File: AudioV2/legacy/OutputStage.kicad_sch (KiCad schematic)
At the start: 7 parts, among them SW501 DEST L (PHONE/MUTE/LINE), SW502 DEST R (PHONE/MUTE/LINE)

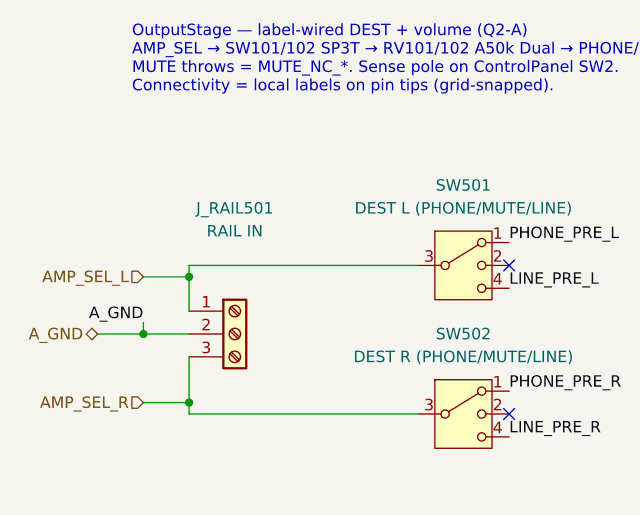
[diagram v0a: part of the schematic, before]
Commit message: AudioV2: レビュー指摘 3・4 を反映（OCP/容量の訂正、旧注釈10個の掃除、J_RAIL501 の Value）
レビューコメント（電源差し替えと U1604 削除の主経路は成立、残る4点は方針/文書/配線手順）
のうち、判断を要しない 3 と 4 を直した。1 と 2 は NOW.md に未判断として置いた。

## 3. DECISIONS の記述訂正（自分の誤り2件）

- U201 の OCP を「150% Io」と書いていたが、それは REC10K の値。
  REC20K-2415DZ は **225% of rated IOUT**（nom. VIN=48VDC、Recom_REC20K-Z_Rev3-2025.pdf）
- 「+15V/-15V とも 259.8µF」は差し替え時点の値。同日の U1604 削除で C1606/C1619
  （計 20.2µF）が中間レールから +15V に載り、いまは **+15V 280.0µF / -15V 259.8µF**。
  REC10K の Cout ±270µF に対して 96% → **103.7% で上限超え**。REC20K の理由②は
  差し替え後にさらに強まった

## 4. MeasureControl の旧注釈を掃除

26 個の text のうち 10 個が 2026-09-01 の再アノテーション前の designator のままだった。
うち3つは内容が現物と食い違っていた:

- [3][4] 電源系の注釈が **削除済みの U1604(MBC2596) の構成を今も説明**していた
  → ⑥-A 後の実配線（ADC の LDO は +15V 直結）に書き直し
- [11] GND の注釈が **NetTie の対応を現物と逆に**書いていた
  （旧「NT702=A_GND─ADC_GND / NT701=ADC_GND_IN─D_GND」→ 現物は NT1601 / NT1602）
  → NT1603 の新設と「3つを近接させる」も足した

残り7個は designator の置換のみ（回路図で1個ずつ対応を確定してから）:
  U704→U1607 U706→U1603 U707→U1606 U708→U1609 U709→U1605
  Y701→Y1601 D701→D1601 A701→A1601
  R717→R1620 R718→R1604 R719→R1611 R720→R1605
  C745→C1614（TPS3307 VDD） C740→C1633（XC8107 CIN） C739→C1631（XC8107 CL）
  NT701→NT1602 NT702→NT1601

同座標・同文の重複 2 組（[13][14] / [15][16]）を1つずつに。残る旧 designator は 0。

## J_RAIL501 の Value

「RAIL IN」→「AMP_SEL OUT」。実ネットは AMP_SEL_L / A_GND / AMP_SEL_R で、
娘基板がスロット直結になる前の名残だった。Description は前回直してある。
Value 変更なので PARTS.md を再生成した（BOM の行が変わる。netlist は変わらない）。

## 1・2 は NOW.md に未判断として置いた

1. ADC 枝の PPTC（旧 F1603）を戻すか — 既に記載あり
2. 計測側の電源端子 J1602/J1603 を残すか — **基板を分けるかの判断の下流**。
   分けないなら J1601 も含めて3個とも不要。分けるなら **J1603 のピン並びが J201 と逆**
   （J201=+15/GND/−15、J1603=−15/GND/+15。ピン番号どおりに繋ぐとレールが入れ替わる）。
   J1602 は F1601 が端子の外側に付いた行き止まりで、⑥-A 後は U1607 1個の 12V 入口

## 検証

  check_sexpr.py -q AudioV2   13 ファイル / 問題 0
  kicad-run.sh erc            11 件（変化なし）
  kicad-run.sh netlist        部品 370 個・重複 0・footprint 未設定 0（変化なし）
  sch_import --roundtrip      6/6 OK
  再生成の冪等性               バイト一致
  gen_parts_bom.py --check    OK

Co-Authored-By: Claude Fabl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
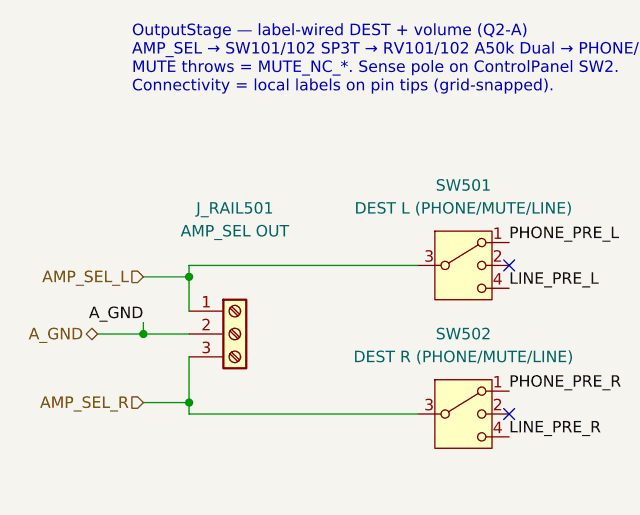
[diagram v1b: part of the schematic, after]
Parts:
- J_RAIL501: value RAIL IN -> AMP_SEL OUT
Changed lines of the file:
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@@
 			)
 		)
-		(property "Value" "RAIL IN"
+		(property "Value" "AMP_SEL OUT"
 			(at 36.83 48.26 0)
 			(show_name no)
@@
 			)
 		)
-		(property "Description" "選択された Amp 出力の取り出し端子。1=AMP_SEL_L / 2=A_GND / 3=AMP_SEL_R で、DEST スイッチ(SW501/SW502)の手前。Value の RAIL IN と旧記述の +12V/A_GND/-12V は、娘基板がスロット直結(J_PWR/J_ANA)になる前の名残で電源ではない。A_GND 極を持つ唯一の音声取り出し口。"
+		(property "Description" "選択された Amp 出力の取り出し端子。1=AMP_SEL_L / 2=A_GND / 3=AMP_SEL_R で、DEST スイッチ(SW501/SW502)の手前。旧 Value の RAIL IN と旧記述の +12V/A_GND/-12V は、娘基板がスロット直結(J_PWR/J_ANA)になる前の名残で電源ではない。A_GND 極を持つ唯一の音声取り出し口。"
 			(at -13.97 -62.23 0)
 			(hide yes)

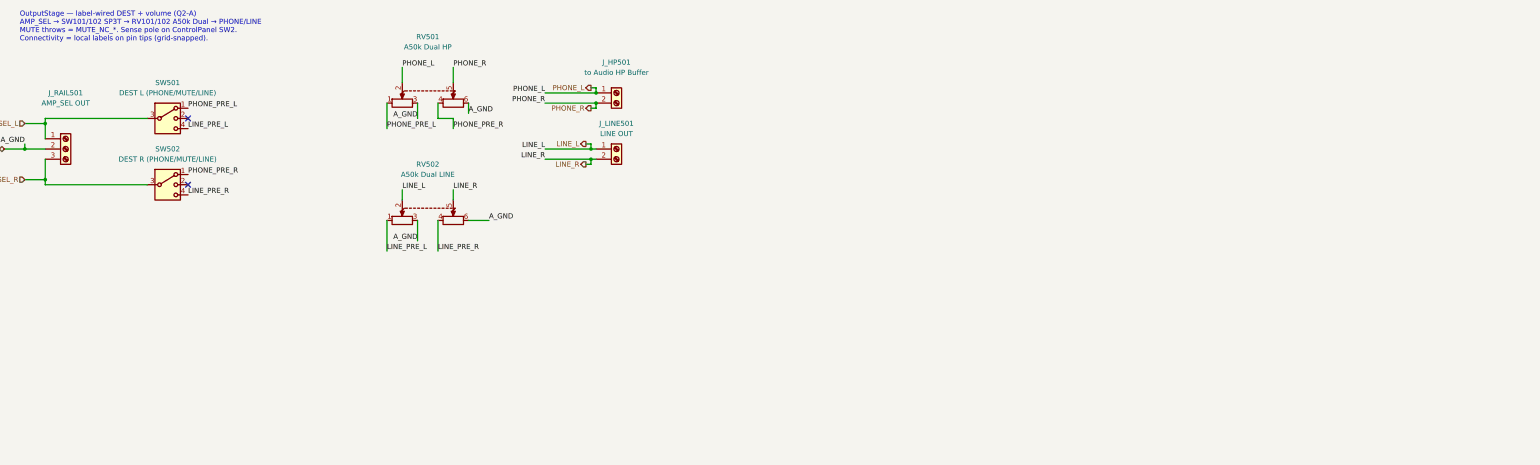
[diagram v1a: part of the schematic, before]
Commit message: AudioV2: HP バッファを移設し、PT2314E の DGND を A_GND へ寄せて I²C にレベルシフタを入れた
未実装のまま「確定」に留まっていた2件を回路図に入れ、注釈・BOM の腐りを直した。

- HP バッファ移設（2026-09-06 確定）: legacy/OutputStage に U501（DIP-8 ソケット、
  標準実装 OPA1652）+ R501/R502 10Ω + C501/C502 470µF NP + R503/R504 100k +
  C503-C506。RV501 ワイパー側のラベルを PHONE_BUF_L/R に改名し、PHONE_L/R は
  バッファ出力になった。J_HP501 / J_LINE501 を 01x03（L / A_GND / R）にして帰路を入れた
- DGND→A_GND ＋ I²C 境界（2026-09-07 確定）: U402.25 を A_GND へ。境界は BSS138 ×2 の
  双方向レベルシフタ（Q401/Q402、PT 側 R412/R413 10k → VCC_TONE）。P82B96 を使わない
  理由（Sx 側 VOL 0.8–1.0 V が PT2314E VIL 1.0 V / RP2350 VIL 0.8 V を食い切る）は
  DECISIONS の実装節に一次資料の数字で置いた
- MeasureControl の注釈: 上書きしてしまった Pico ピン配置ノートを復元（GP9=NC）、
  R1605 / 3.3k の旧記述を消し、U1611 Description を実値（約30k・−115.5 dB）に直した
- NT1603 を in_bom no に揃え、PARTS.md は 385（ネットリスト 389 − NetTie 4）
- DECISIONS: PPTC「戻さない」の理由を言い直し（1・2行目は判定材料にならない、
  3行目の条件は X7R 割れに限らない、U201 の OCP は 230 % max @ nom. VIN 24 V）、
  ヘッドルーム −0.4 dBFS は typ 基準で余裕の確定ではないと追記（7.5k 案を併記）、
  U1611 の 47Ω 省略に CL 100 pF の根拠を足した

検証: check_sexpr 0 / roundtrip 全 OK / 再生成は冪等（バイト一致）/ ERC 11 件（型・件数とも
変化なし）/ ネットリスト 389 個・重複 0・フットプリント未設定 0 / 母板で座標の偶然一致なし

Co-Authored-By: Claude Fable 5.1 <noreply@anthropic.com>
Claude-Session: https://claude.ai/code/session_01VCArLcCGbMGgxvWJ5HFJiY
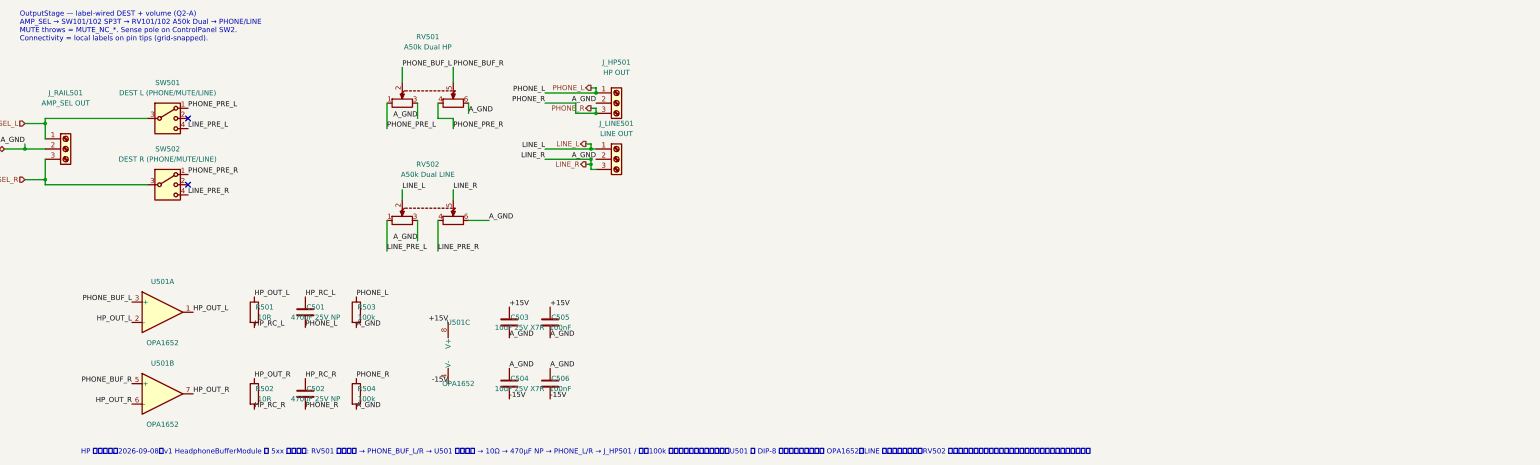
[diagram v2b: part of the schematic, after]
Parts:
- added C501, C502: 470uF 25V NP, Capacitor_THT:CP_Radial_D10.0mm_P5.00mm, symbol Device:C
- added C503, C504: 10uF 25V X7R, Capacitor_SMD:C_1206_3216Metric_Pad1.33x1.80mm_HandSolder, symbol Device:C
- added C505, C506: 100nF, Capacitor_SMD:C_1206_3216Metric_Pad1.33x1.80mm_HandSolder, symbol Device:C
- added R501, R502: 10R, Resistor_SMD:R_1206_3216Metric_Pad1.30x1.75mm_HandSolder, symbol Device:R
- added R503, R504: 100k, Resistor_SMD:R_1206_3216Metric_Pad1.30x1.75mm_HandSolder, symbol Device:R
- added U501: OPA1652, Package_DIP:DIP-8_W7.62mm_Socket, symbol Amplifier_Operational:NE5532
- J_HP501: value to Audio HP Buffer -> HP OUT; footprint TerminalBlock_Phoenix:TerminalBlock_Phoenix_MKDS-1,5-2-5.08_1x02_P5.08mm_Horizontal -> TerminalBlock_Phoenix:TerminalBlock_Phoenix_MKDS-1,5-3-5.08_1x03_P5.08mm_Horizontal; symbol Connector:Screw_Terminal_01x02 -> Connector:Screw_Terminal_01x03
- J_LINE501: footprint TerminalBlock_Phoenix:TerminalBlock_Phoenix_MKDS-1,5-2-5.08_1x02_P5.08mm_Horizontal -> TerminalBlock_Phoenix:TerminalBlock_Phoenix_MKDS-1,5-3-5.08_1x03_P5.08mm_Horizontal; symbol Connector:Screw_Terminal_01x02 -> Connector:Screw_Terminal_01x03
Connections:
- net A_GND: now also J_HP501.2 (Pin_2), J_LINE501.2 (Pin_2), C503.2, C504.1, C505.2, C506.1, R503.2, R504.2
- net LINE_R: now also J_LINE501.3 (Pin_3); no longer J_LINE501.2 (Pin_2)
- net PHONE_L: now also C501.2, R503.1; no longer RV501.2
- net PHONE_R: now also J_HP501.3 (Pin_3), C502.2, R504.1; no longer J_HP501.2 (Pin_2), RV501.5
- new net +15V: C503.1, C505.1, U501.8 (V+)
- new net -15V: C504.2, C506.2, U501.4 (V-)
- new net HP_OUT_L: R501.1, U501.1, U501.2 (-)
- new net HP_OUT_R: R502.1, U501.6 (-), U501.7
- new net HP_RC_L: C501.1, R501.2
- new net HP_RC_R: C502.1, R502.2
- new net PHONE_BUF_L: RV501.2, U501.3 (+)
- new net PHONE_BUF_R: RV501.5, U501.5 (+)
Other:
- note added: "HP バッファ（2026-09-08、v1 HeadphoneBufferModule を 5xx で移設）: RV501 ワイパー → PHONE_BUF_L/R → U501 ユニティ → 10Ω → 470µF NP → PHONE_L/R → J_HP501 / 親。100k はジャック側のブリード。U501 は DIP-8 ソケット、標準実装 OPA1652。LINE はバッファ無し（RV502 直出し）のまま。配線はピン先ラベル（このシートの流儀）。"

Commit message: AudioV2: C501/C502 を Ø16/P7.5 に（Muse ES 470µF が入る）
HP 出力の無極性ブロックを UES1E471MHM クラスの寸法に合わせた。

Co-authored-by: Cursor <cursoragent@cursor.com>
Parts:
- C501, C502: footprint Capacitor_THT:CP_Radial_D10.0mm_P5.00mm -> Capacitor_THT:CP_Radial_D16.0mm_P7.50mm
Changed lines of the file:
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@@
 			)
 		)
-		(property "Footprint" "Capacitor_THT:CP_Radial_D10.0mm_P5.00mm"
+		(property "Footprint" "Capacitor_THT:CP_Radial_D16.0mm_P7.50mm"
 			(at 96.52 100.33 0)
 			(hide yes)
@@
 			)
 		)
-		(property "Description" "HP 出力の DC ブロック（v1 C901）。無極性電解。役目はオフセットではなく素子故障時の保護（DECISIONS）"
+		(property "Description" "HP 出力の DC ブロック（v1 C901）。無極性電解。役目はオフセットではなく素子故障時の保護（DECISIONS）。FP は Ø16/P7.5（2026-09-10）— Muse ES UES1E471MHM（470µF 25V BP）が入るサイズ"
 			(at 96.52 100.33 0)
 			(hide yes)
@@
 			)
 		)
-		(property "Footprint" "Capacitor_THT:CP_Radial_D10.0mm_P5.00mm"
+		(property "Footprint" "Capacitor_THT:CP_Radial_D16.0mm_P7.50mm"
 			(at 96.52 120.65 0)
 			(hide yes)
@@
 			)
 		)
-		(property "Description" "HP 出力の DC ブロック（v1 C902）。無極性電解"
+		(property "Description" "HP 出力の DC ブロック（v1 C902）。無極性電解。FP は Ø16/P7.5（2026-09-10）— Muse ES UES1E471MHM（470µF 25V BP）が入るサイズ"
 			(at 96.52 120.65 0)
 			(hide yes)
